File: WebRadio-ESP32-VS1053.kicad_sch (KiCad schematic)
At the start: 72 parts, among them J1 Conn_01x02, J2 Conn_01x02_Pin, J3 Conn_01x02_Pin, J4 AudioJack3, J5 Conn_01x02_Pin, SW1 SW_Push, SW2 SW_Push, SW3 SW_Push, SW4 SW_Push, U1 AMS1117-1.8, U2 mini_esp32, U4 VS1053b, U5 JLCPCB Marker, U6 PAM8403D, Y1 12,288MHz

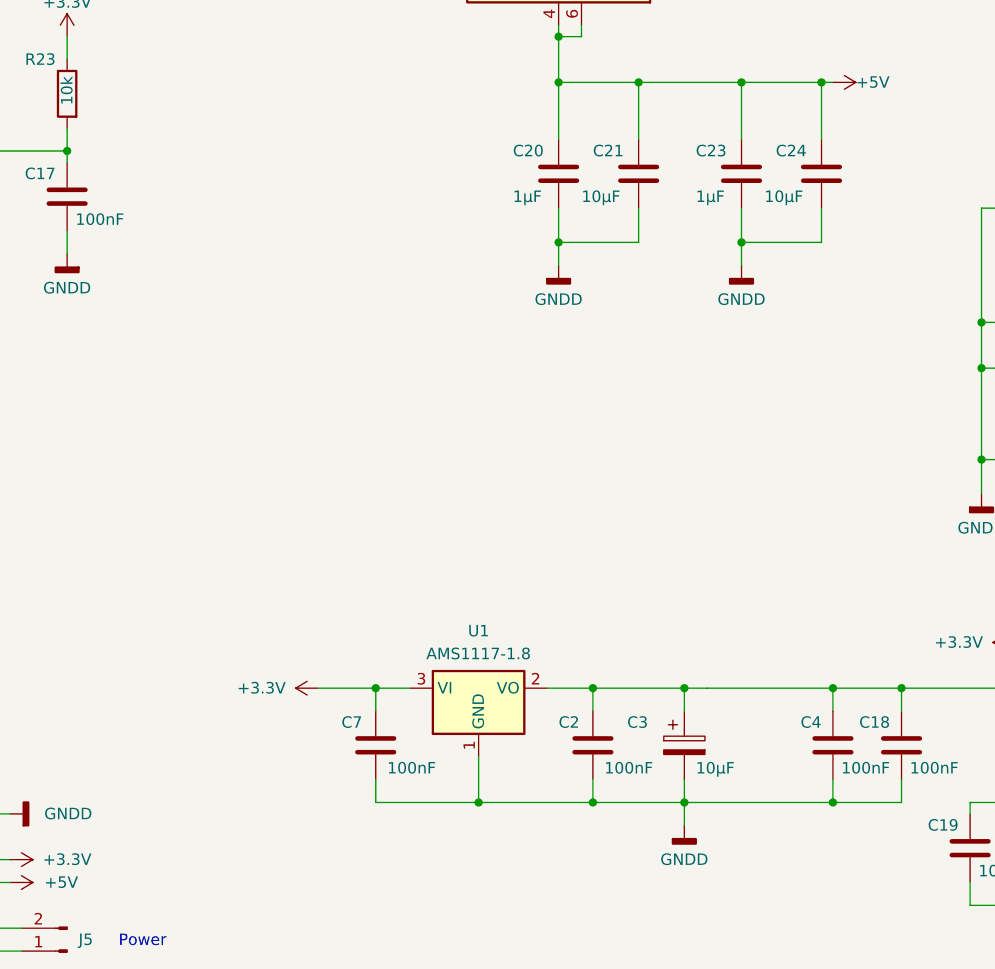
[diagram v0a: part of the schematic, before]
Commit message: include power over usb-c and jst connector
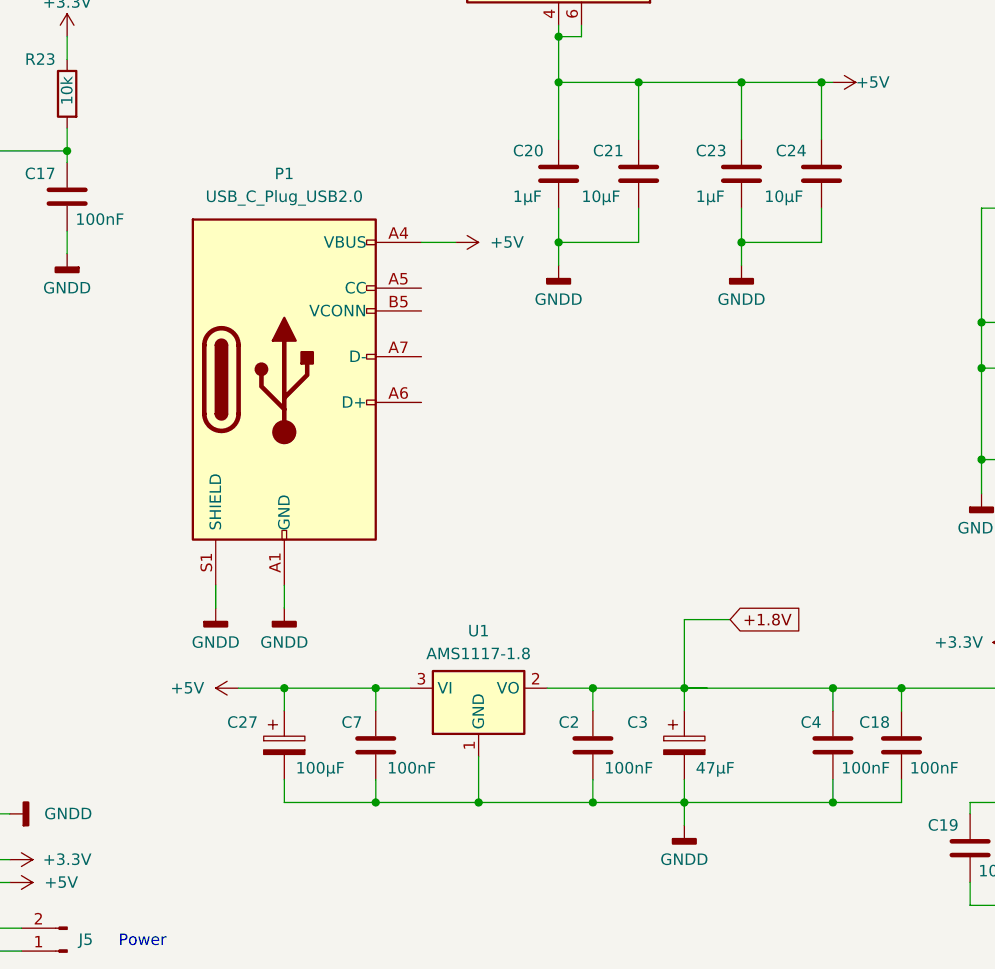
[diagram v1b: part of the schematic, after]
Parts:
- added C27: 100µF, Capacitor_SMD_AKL:CP_Elec_5x5.7, symbol Library:CP_SMD_D5.0mm_H5.7mm
- added P1: USB_C_Plug_USB2.0, Connector_USB:USB_C_Receptacle_GCT_USB4125-xx-x_6P_TopMnt_Horizontal, symbol Connector:USB_C_Plug_USB2.0
- C1, C10, C11, C12, C13, C14, C15, C16, C17, C18, C19, C2, C20, C21, C22, C23, C24, C25, C26, C4, C5, C6, C7, C8, C9: symbol Device:C -> Library:C
- C3: value 10µF -> 47µF; footprint Capacitor_SMD:CP_Elec_4x5.4 -> Capacitor_SMD_AKL:CP_Elec_5x5.7; symbol PCM_Capacitor_AKL:CP_SMD_D5.0mm_H5.7mm -> Library:CP_SMD_D5.0mm_H5.7mm
- D1, D2, D3, D4: symbol Device:LED -> Library:LED
- DS2: footprint psch:TFT2.2_SPI_5P_SD -> psch:TFT2.2_SPI_4P_SD; symbol psch:TFT2.2_SPI_4P_SD -> Library:TFT2.2_SPI_4P_SD
- H1, H2, H3, H4: footprint MountingHole:MountingHole_3.2mm_M3_ISO7380 -> MountingHole:MountingHole_3.2mm_M3_ISO14580; symbol Mechanical:MountingHole -> Library:MountingHole
- J1: symbol Connector_Generic:Conn_01x02 -> Library:Conn_01x02
- J2, J3, J5: symbol Connector:Conn_01x02_Pin -> Library:Conn_01x02_Pin
- J4: footprint psch:Jack_3.5mm_SMT_Horizontal -> lib_psch:Jack_3.5mm_SMT_Horizontal; symbol Connector_Audio:AudioJack3 -> Library:AudioJack3
- R1, R10, R11, R12, R13, R14, R15, R16, R17, R18, R19, R2, R20, R21, R23, R3, R4, R5, R6, R7, R8, R9: symbol Device:R -> Library:R
- SW1, SW2, SW3, SW4: symbol Switch:SW_Push -> Library:SW_Push
- U1: symbol Regulator_Linear:AMS1117-1.8 -> Library:AMS1117-1.8
- U2: footprint esp32-mini:ESP32_mini -> ESP32_mini:ESP32_mini; symbol esp32-mini:mini_esp32 -> Library:mini_esp32
- U4: symbol psch:VS1053b -> Library:VS1053b
- U5: footprint psch:JLCPCB-Marker -> lib_psch:JLCPCB-Marker; symbol psch:JLCPCB -> Library:JLCPCB
- U6: symbol Amplifier_Audio:PAM8403D -> Library:PAM8403D
- Y1: symbol Device:Crystal_Small -> Library:Crystal_Small
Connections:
- net +3.3V: no longer C7.1, U1.3 (VI)
- net +5V: now also C7.1, U1.3 (VI), C27.1, P1.A4 (VBUS), P1.A9 (VBUS), P1.B4 (VBUS), P1.B9 (VBUS)
- net GNDD: now also C27.2, P1.A1 (GND), P1.A12 (GND), P1.B1 (GND), P1.B12 (GND), P1.S1 (SHIELD)
- net +1.8V: now reaches C18.2, C2.1, C3.1, C4.2, U1.2 (VO), U4.24 (CVDD2), U4.31 (CVDD3), U4.5 (CVDD0), U4.7 (CVDD1)

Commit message: change some comments
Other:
- note added: "lowpass filter"
- note removed: "Tiefpass ca. 16kHz"
- title: VS1053b Streaming -> WebRadio ESP32
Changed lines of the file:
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@@
 	(paper "A4")
 	(title_block
-		(title "VS1053b Streaming")
+		(title "WebRadio ESP32")
 		(date "2024-03-17")
-		(rev "1.0")
+		(rev "1.2")
 		(company "PSch")
 	)
@@
 		)
 	)
-	(text "Tiefpass ca. 16kHz"
+	(text "lowpass filter"
 		(exclude_from_sim no)
 		(at 113.538 21.082 0)

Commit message: add new footrint for 3mm LED to us also SMD LED's
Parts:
- D1, D2, D3: footprint LED_THT:LED_D3.0mm -> lib_psch:LED_D3.0mm_SMD
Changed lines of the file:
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@@
 			)
 		)
-		(property "Footprint" "LED_THT:LED_D3.0mm"
+		(property "Footprint" "lib_psch:LED_D3.0mm_SMD"
 			(at 54.61 185.42 0)
 			(effects
@@
 			)
 		)
-		(property "Description" ""
+		(property "Description" "USB 2.0-only Type-C Plug connector"
 			(at 109.22 90.17 0)
 			(effects
@@
 			)
 		)
-		(property "Footprint" "LED_THT:LED_D3.0mm"
+		(property "Footprint" "lib_psch:LED_D3.0mm_SMD"
 			(at 54.61 179.07 0)
 			(effects
@@
 			)
 		)
-		(property "Footprint" "LED_THT:LED_D3.0mm"
+		(property "Footprint" "lib_psch:LED_D3.0mm_SMD"
 			(at 54.61 172.72 0)
 			(effects

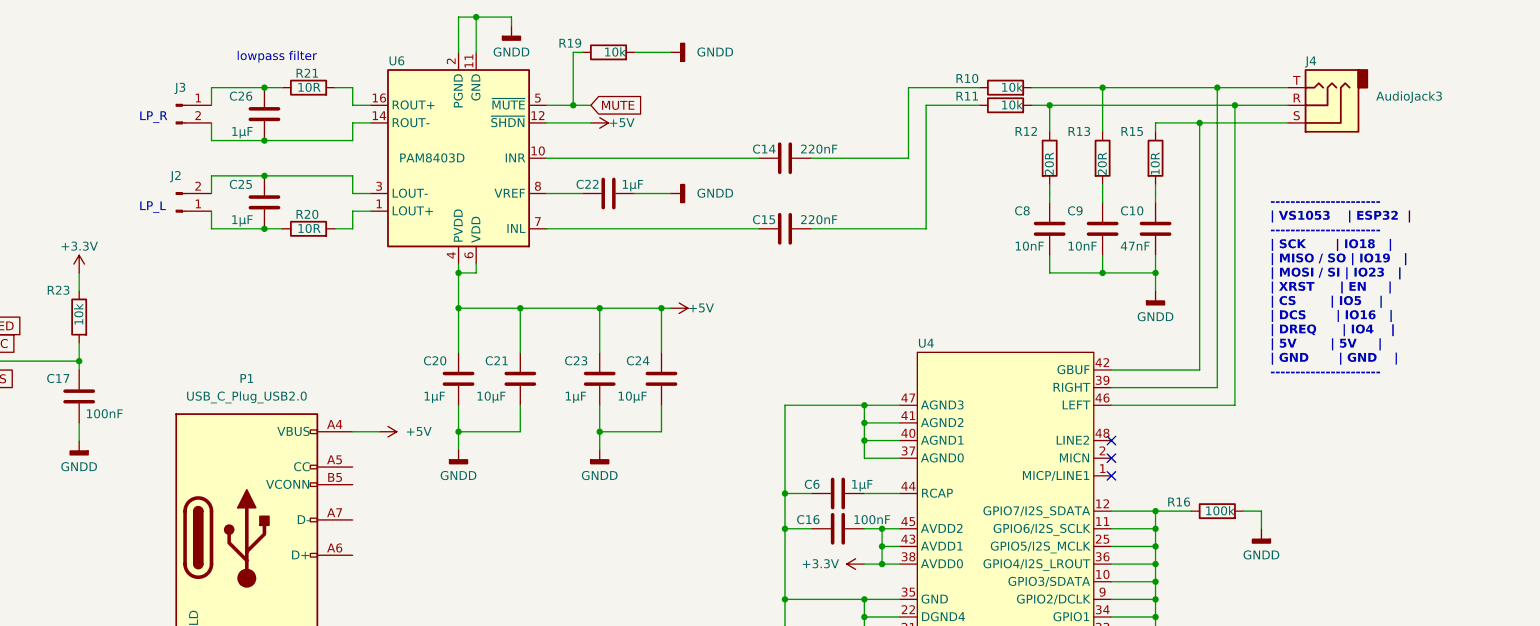
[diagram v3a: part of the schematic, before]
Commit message: add audio output connector
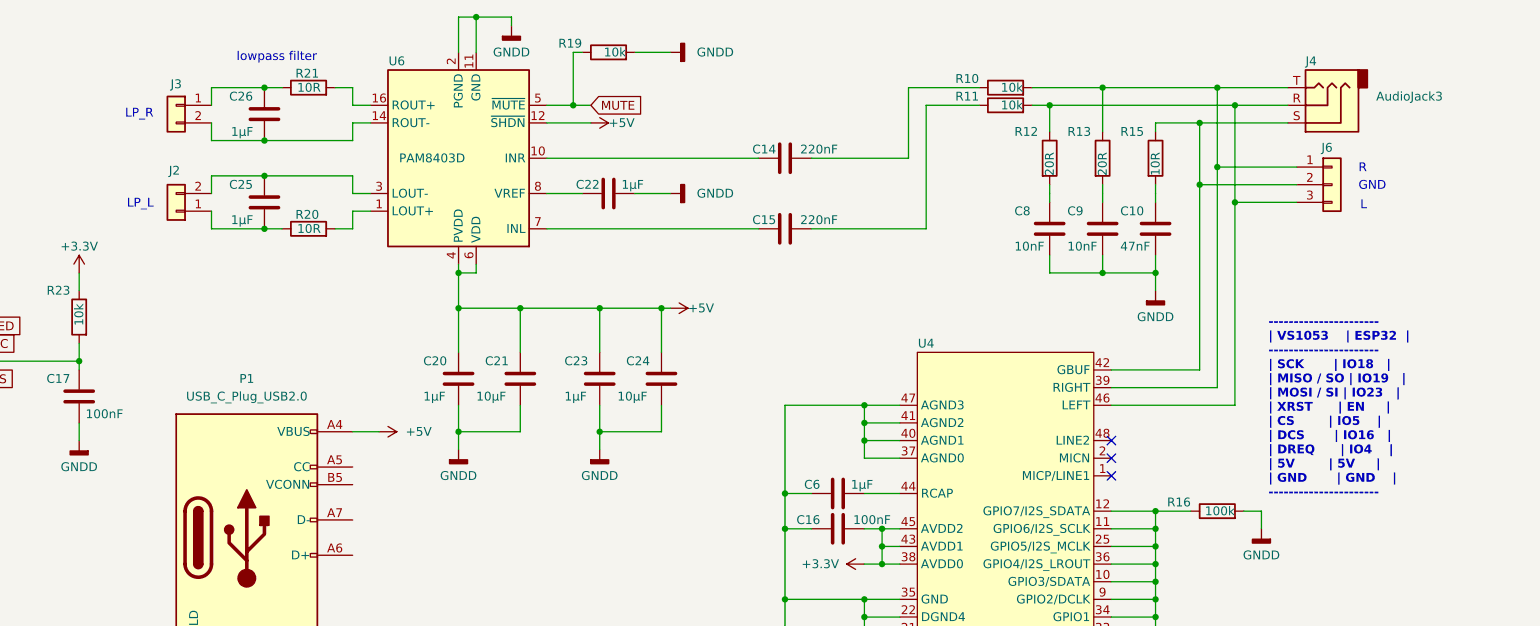
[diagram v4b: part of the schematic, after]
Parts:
- removed J2, J3: Conn_01x02_Pin, Connector_JST:JST_PH_B2B-PH-K_1x02_P2.00mm_Vertical, symbol Library:Conn_01x02_Pin
- added J2, J3: JST PH 2mm, Connector_JST:JST_PH_B2B-PH-K_1x02_P2.00mm_Vertical, symbol Connector_Generic:Conn_01x02
- added J6: JST PH 2mm, Connector_JST:JST_PH_B3B-PH-K_1x03_P2.00mm_Vertical, symbol Connector_Generic:Conn_01x03
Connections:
- net at J4.R, R11.2, R12.1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: now also J6.3 (Pin_3)
- net at J4.T, R10.2, R13.1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: now also J6.1 (Pin_1)
- net at J4.S, R15.1, U4.42 (GBUF): now also J6.2 (Pin_2)
- net at C26.1, R21.1: now also J3.1 (Pin_1)
- net at C26.2, U6.14 (ROUT-): now also J3.2 (Pin_2)
- net at C25.1, U6.3 (LOUT-): now also J2.2 (Pin_2)
- net at C25.2, R20.1: now also J2.1 (Pin_1)
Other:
- note added: "GND"
- note added: "L"
- note added: "R"
